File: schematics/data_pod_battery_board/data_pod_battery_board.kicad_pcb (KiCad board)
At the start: 2 copper layers, 292.1 x 292.1 mm, 80 parts, among them J1 Conn_01x02, J10 Screw_Terminal_01x01, J11 Screw_Terminal_01x01, J12 Screw_Terminal_01x01, J13 Screw_Terminal_01x01, J14 Screw_Terminal_01x01, J15 Screw_Terminal_01x01, J16 Screw_Terminal_01x01, J17 Screw_Terminal_01x01, J18 Screw_Terminal_01x01, J19 Screw_Terminal_01x01, J2 Screw_Terminal_01x01, J20 Screw_Terminal_01x01, J21 Screw_Terminal_01x01, J22 Screw_Terminal_01x01, J23 Screw_Terminal_01x01, J24 Screw_Terminal_01x01, J25 Screw_Terminal_01x01, J26 Screw_Terminal_01x01, J27 Screw_Terminal_01x01, J28 Screw_Terminal_01x01, J29 Screw_Terminal_01x01, J3 Screw_Terminal_01x01, J30 Screw_Terminal_01x01, J31 Screw_Terminal_01x01, J32 Screw_Terminal_01x01, J33 Screw_Terminal_01x01, J34 Conn_01x02, J35 Screw_Terminal_01x01, J36 Screw_Terminal_01x01, J37 Screw_Terminal_01x01, J38 Screw_Terminal_01x01, J39 Screw_Terminal_01x01, J4 Screw_Terminal_01x01, J40 Screw_Terminal_01x01, J41 Screw_Terminal_01x01, J42 Screw_Terminal_01x01, J43 Screw_Terminal_01x01, J44 Screw_Terminal_01x01, J45 Screw_Terminal_01x01, J46 Screw_Terminal_01x01, J47 Screw_Terminal_01x01, J48 Screw_Terminal_01x01, J49 Screw_Terminal_01x01, J5 Screw_Terminal_01x01, J50 Screw_Terminal_01x01, J6 Screw_Terminal_01x01, J7 Screw_Terminal_01x01, J8 Screw_Terminal_01x01, J9 Screw_Terminal_01x01

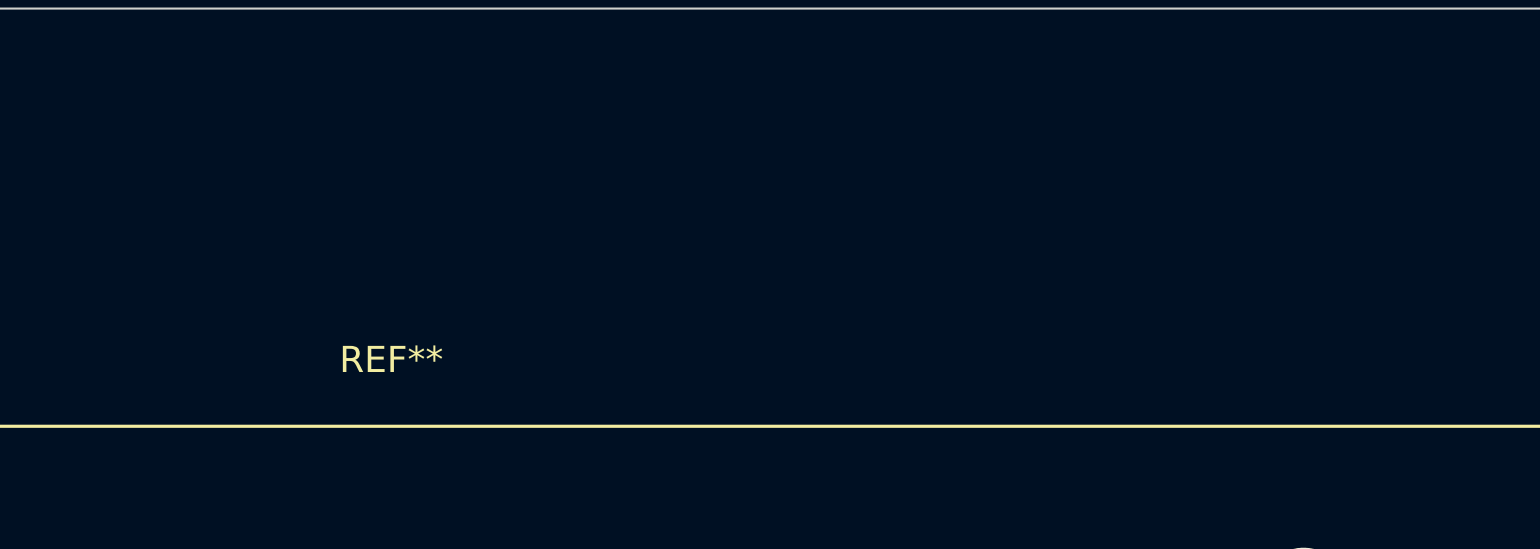
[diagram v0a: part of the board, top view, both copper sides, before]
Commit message: added text the pcb rev2
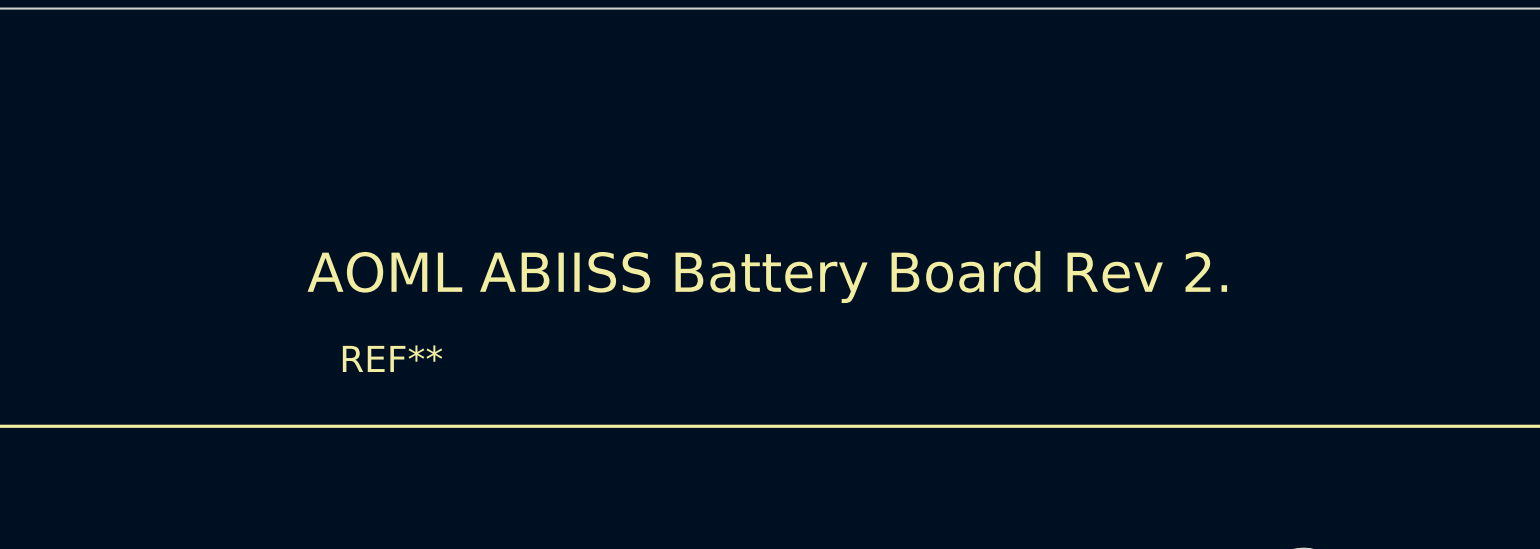
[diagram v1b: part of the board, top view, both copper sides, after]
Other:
- board text added: "AOML ABIISS Battery Board Rev 2."
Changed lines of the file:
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@@
   (general
     (thickness 1.6)
-    (drawings 9)
+    (drawings 10)
     (tracks 421)
     (zones 0)
@@
     )
   )
+  (gr_text "AOML ABIISS Battery Board Rev 2." (at 344.293154 63.947848) (layer F.SilkS)
+    (effects (font (size 1.5 1.5) (thickness 0.375)))
+  )
   (target plus (at 108.708154 53.787848) (size 5) (width 0.05) (layer Edge.Cuts))
